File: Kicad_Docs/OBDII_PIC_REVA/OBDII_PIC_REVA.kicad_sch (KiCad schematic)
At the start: 11 parts, among them SW1 SW_MEC_5G, SW2 SW_MEC_5G, U1 RC1602A-GHW-ESX, U2 PIC18F46K22-I_P, U3 STN1110

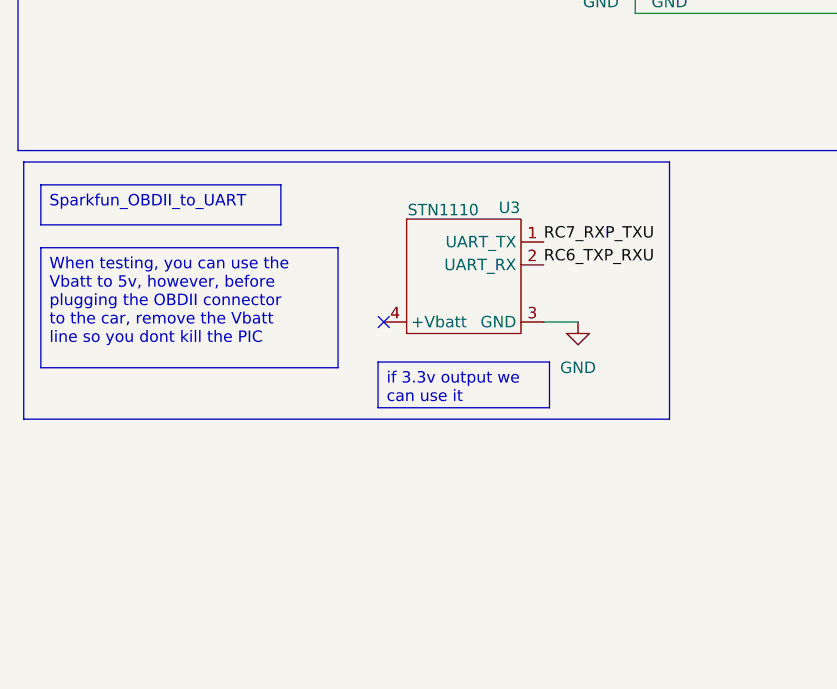
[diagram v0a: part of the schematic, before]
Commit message: Updated README.md, added some changes to schematic, cleaned up the project presentation
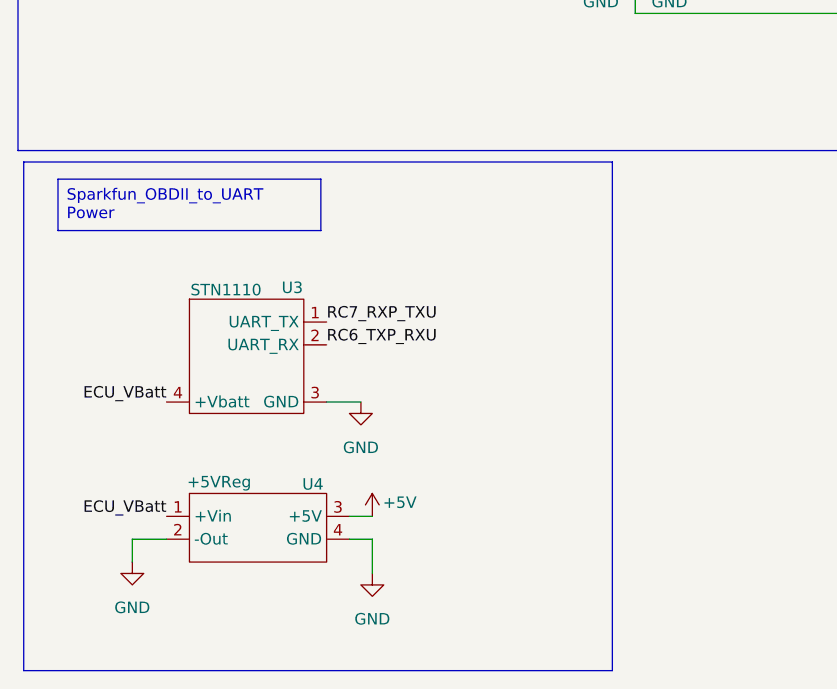
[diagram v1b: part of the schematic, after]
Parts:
- added U4: +5VReg, symbol 5vReg:5vReg
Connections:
- net +5V: now also U4.3 (+5V)
- net GND: now also U4.2 (-Out), U4.4 (GND)
- net ECU_VBatt: now reaches U3.4 (+Vbatt)
- net ECU_VBatt: now also U4.1 (+Vin)
- no-connect marks 28 -> 27
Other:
- moved on the sheet: U3
